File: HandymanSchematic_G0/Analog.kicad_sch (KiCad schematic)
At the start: 62 parts, among them Q1 BC847, Q2 BC847, U1 TL074, U2 TL074, U3 TL072

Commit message: rough layout
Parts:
- TP1: value AC -> AK
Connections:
- net AmpAnode: now also U2.14; no longer U2.7
- net at R19.2, R21.1: now also U2.9 (-); no longer U2.13 (-)
- net at R18.2, R20.1: now also U2.13 (-); no longer U2.6 (-)
- net at R11.1, R9.2: now also U2.6 (-); no longer U2.9 (-)
- net at R11.2, R14.1: now also U2.7; no longer U2.8
- net at C11.1, R21.2: now also U2.8; no longer U2.14
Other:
- moved on the sheet: U2B, U2C, U2D
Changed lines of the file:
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@@
 	)
 	(junction
-		(at 130.81 198.12)
-		(diameter 0)
-		(color 0 0 0 0)
-	)
-	(junction
 		(at 142.24 67.31)
 		(diameter 0)
@@
 	)
 	(junction
+		(at 181.61 200.66)
+		(diameter 0)
+		(color 0 0 0 0)
+	)
+	(junction
 		(at 49.53 67.31)
 		(diameter 0)
@@
 	)
 	(junction
+		(at 130.81 198.12)
+		(diameter 0)
+		(color 0 0 0 0)
+	)
+	(junction
+		(at 181.61 168.91)
+		(diameter 0)
+		(color 0 0 0 0)
+	)
+	(junction
 		(at 111.76 195.58)
 		(diameter 0)
@@
 	)
 	(junction
-		(at 181.61 168.91)
-		(diameter 0)
-		(color 0 0 0 0)
-	)
-	(junction
-		(at 181.61 200.66)
-		(diameter 0)
-		(color 0 0 0 0)
-	)
-	(junction
 		(at 121.92 163.83)
 		(diameter 0)
@@
 	(rectangle
 		(start 236.474 119.126)
-		(end 265.938 158.75)
+		(end 269.748 158.75)
 		(stroke
 			(width 0)
@@
 		(fields_autoplaced yes)
 		(property "Reference" "TP1"
-			(at 242.824 122.1739 0)
+			(at 243.84 122.1739 0)
 			(effects
 				(font
@@
 			)
 		)
-		(property "Value" "AC"
-			(at 242.824 124.7139 0)
+		(property "Value" "AK"
+			(at 243.84 124.7139 0)
 			(effects
 				(font
@@
 	(symbol
 		(lib_id "Amplifier_Operational:TL074")
-		(at 173.99 168.91 0)
+		(at 123.19 198.12 0)
 		(mirror x)
 		(unit 2)
@@
 		(dnp no)
 		(property "Reference" "U2"
-			(at 173.99 179.07 0)
+			(at 123.19 208.28 0)
 			(effects
 				(font
@@
 		)
 		(property "Value" "TL074"
-			(at 173.99 176.53 0)
+			(at 123.19 205.74 0)
 			(effects
 				(font
@@
 		)
 		(property "Footprint" "Package_SO:SOIC-14_3.9x8.7mm_P1.27mm"
-			(at 172.72 171.45 0)
+			(at 121.92 200.66 0)
 			(effects
 				(font
@@
 		)
 		(property "Datasheet" "http://www.ti.com/lit/ds/symlink/tl071.pdf"
-			(at 175.26 173.99 0)
+			(at 124.46 203.2 0)
 			(effects
 				(font
@@
 		)
 		(property "Description" "Quad Low-Noise JFET-Input Operational Amplifiers, DIP-14/SOIC-14"
-			(at 173.99 168.91 0)
+			(at 123.19 198.12 0)
 			(effects
 				(font
@@
 	(symbol
 		(lib_id "Amplifier_Operational:TL074")
-		(at 173.99 200.66 0)
+		(at 173.99 168.91 0)
 		(mirror x)
 		(unit 4)
@@
 		(dnp no)
 		(property "Reference" "U2"
-			(at 173.99 210.82 0)
+			(at 173.99 179.07 0)
 			(effects
 				(font
@@
 		)
 		(property "Value" "TL074"
-			(at 173.99 208.28 0)
+			(at 173.99 176.53 0)
 			(effects
 				(font
@@
 		)
 		(property "Footprint" "Package_SO:SOIC-14_3.9x8.7mm_P1.27mm"
-			(at 172.72 203.2 0)
+			(at 172.72 171.45 0)
 			(effects
 				(font
@@
 		)
 		(property "Datasheet" "http://www.ti.com/lit/ds/symlink/tl071.pdf"
-			(at 175.26 205.74 0)
+			(at 175.26 173.99 0)
 			(effects
 				(font
@@
 		)
 		(property "Description" "Quad Low-Noise JFET-Input Operational Amplifiers, DIP-14/SOIC-14"
-			(at 173.99 200.66 0)
+			(at 173.99 168.91 0)
 			(effects
 				(font
@@
 	(symbol
 		(lib_id "Amplifier_Operational:TL074")
-		(at 123.19 198.12 0)
+		(at 173.99 200.66 0)
 		(mirror x)
 		(unit 3)
@@
 		(dnp no)
 		(property "Reference" "U2"
-			(at 123.19 208.28 0)
+			(at 173.99 210.82 0)
 			(effects
 				(font
@@
 		)
 		(property "Value" "TL074"
-			(at 123.19 205.74 0)
+			(at 173.99 208.28 0)
 			(effects
 				(font
@@
 		)
 		(property "Footprint" "Package_SO:SOIC-14_3.9x8.7mm_P1.27mm"
-			(at 121.92 200.66 0)
+			(at 172.72 203.2 0)
 			(effects
 				(font
@@
 		)
 		(property "Datasheet" "http://www.ti.com/lit/ds/symlink/tl071.pdf"
-			(at 124.46 203.2 0)
+			(at 175.26 205.74 0)
 			(effects
 				(font
@@
 		)
 		(property "Description" "Quad Low-Noise JFET-Input Operational Amplifiers, DIP-14/SOIC-14"
-			(at 123.19 198.12 0)
+			(at 173.99 200.66 0)
 			(effects
 				(font

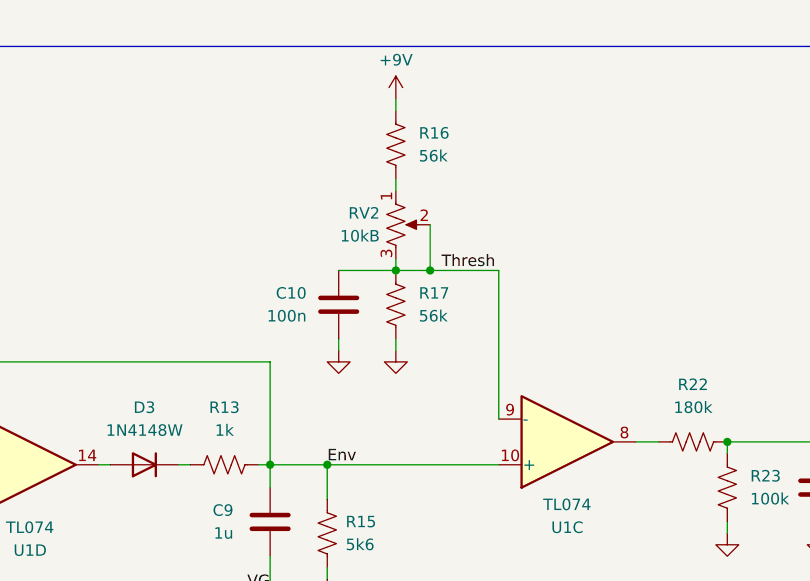
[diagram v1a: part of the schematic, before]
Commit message: removed unused components
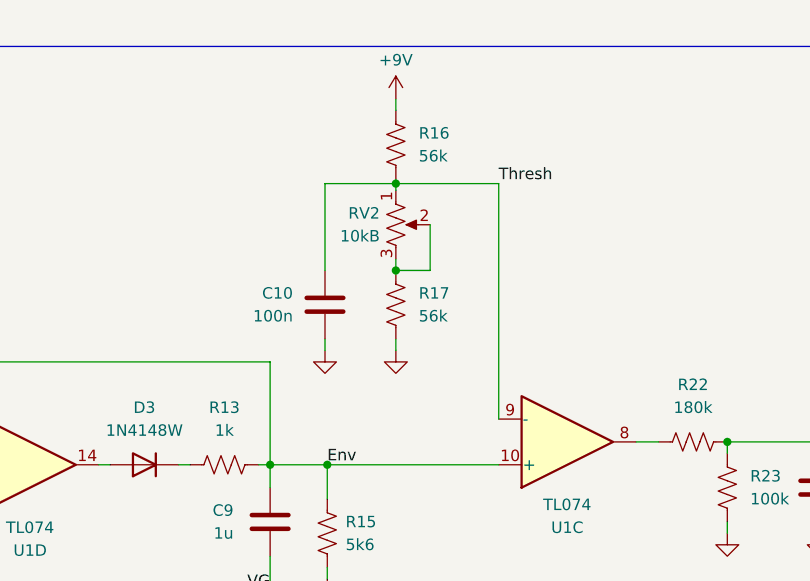
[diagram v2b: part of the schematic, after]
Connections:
- net Thresh: now also R16.2, RV2.1; no longer R17.1, RV2.2, RV2.3
- new net: R17.1, RV2.2, RV2.3
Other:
- moved on the sheet: C10
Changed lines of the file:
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@@
 	)
 	(junction
-		(at 294.132 62.23)
+		(at 149.86 36.068)
 		(diameter 0)
 		(color 0 0 0 0)
 	)
 	(junction
-		(at 69.85 201.93)
+		(at 294.132 62.23)
 		(diameter 0)
 		(color 0 0 0 0)
 	)
 	(junction
-		(at 153.67 45.72)
+		(at 69.85 201.93)
 		(diameter 0)
 		(color 0 0 0 0)
@@
 	(wire
 		(pts
-			(xy 161.29 62.23) (xy 161.29 45.72)
+			(xy 161.29 36.068) (xy 161.29 62.23)
 		)
 		(stroke
@@
 	(wire
 		(pts
-			(xy 149.86 35.56) (xy 149.86 36.83)
+			(xy 149.86 35.56) (xy 149.86 36.068)
 		)
 		(stroke
@@
 	(wire
 		(pts
-			(xy 161.29 45.72) (xy 153.67 45.72)
-		)
-		(stroke
-			(width 0)
-			(type default)
-		)
-	)
-	(wire
-		(pts
 			(xy 186.69 64.77) (xy 186.69 66.04)
 		)
@@
 	(wire
 		(pts
-			(xy 304.546 62.23) (xy 317.246 62.23)
+			(xy 161.29 36.068) (xy 149.86 36.068)
 		)
 		(stroke
@@
 	(wire
 		(pts
-			(xy 170.18 190.5) (xy 162.56 190.5)
+			(xy 304.546 62.23) (xy 317.246 62.23)
 		)
 		(stroke
@@
 	(wire
 		(pts
-			(xy 170.18 158.75) (xy 162.56 158.75)
+			(xy 170.18 190.5) (xy 162.56 190.5)
 		)
 		(stroke
@@
 	(wire
 		(pts
-			(xy 304.546 62.23) (xy 304.546 64.77)
+			(xy 170.18 158.75) (xy 162.56 158.75)
 		)
 		(stroke
@@
 	(wire
 		(pts
-			(xy 143.51 45.72) (xy 149.86 45.72)
+			(xy 304.546 62.23) (xy 304.546 64.77)
 		)
 		(stroke
@@
 	(wire
 		(pts
+			(xy 149.86 36.068) (xy 149.86 36.83)
+		)
+		(stroke
+			(width 0)
+			(type default)
+		)
+	)
+	(wire
+		(pts
 			(xy 177.8 158.75) (xy 181.61 158.75)
 		)
@@
 	(wire
 		(pts
-			(xy 143.51 53.34) (xy 143.51 54.61)
+			(xy 141.986 53.34) (xy 141.986 54.61)
 		)
 		(stroke
@@
 	(wire
 		(pts
+			(xy 141.986 45.72) (xy 141.986 36.068)
+		)
+		(stroke
+			(width 0)
+			(type default)
+		)
+	)
+	(wire
+		(pts
 			(xy 49.53 59.69) (xy 54.61 59.69)
 		)
@@
 	(wire
 		(pts
+			(xy 141.986 36.068) (xy 149.86 36.068)
+		)
+		(stroke
+			(width 0)
+			(type default)
+		)
+	)
+	(wire
+		(pts
 			(xy 107.95 93.98) (xy 125.73 93.98)
 		)
@@
 	(label "VG"
 		(at 123.19 168.91 180)
+		(fields_autoplaced yes)
 		(effects
 			(font
@@
 	(label "VG"
 		(at 135.89 81.28 180)
+		(fields_autoplaced yes)
 		(effects
 			(font
@@
 	(label "AmpAnode"
 		(at 246.126 133.604 0)
+		(fields_autoplaced yes)
 		(effects
 			(font
@@
 	(label "VG"
 		(at 95.25 177.8 0)
+		(fields_autoplaced yes)
 		(effects
 			(font
@@
 	(label "VG"
 		(at 50.8 72.39 180)
+		(fields_autoplaced yes)
 		(effects
 			(font
@@
 	(label "Env"
 		(at 142.24 67.31 0)
+		(fields_autoplaced yes)
 		(effects
 			(font
@@
 		)
 	)
-	(label "HalfRect"
-		(at 80.01 60.96 0)
+	(label "Thresh"
+		(at 161.29 36.068 0)
+		(fields_autoplaced yes)
 		(effects
 			(font
@@
 		)
 	)
-	(label "VG"
-		(at 142.24 90.17 180)
+	(label "HalfRect"
+		(at 80.01 60.96 0)
+		(fields_autoplaced yes)
 		(effects
 			(font
 				(size 1.27 1.27)
 			)
-			(justify right bottom)
+			(justify left bottom)
 		)
 	)
 	(label "VG"
-		(at 95.25 82.55 180)
+		(at 142.24 90.17 180)
+		(fields_autoplaced yes)
 		(effects
 			(font
@@
 		)
 	)
-	(label "Thresh"
-		(at 154.94 45.72 0)
+	(label "VG"
+		(at 95.25 82.55 180)
+		(fields_autoplaced yes)
 		(effects
 			(font
 				(size 1.27 1.27)
 			)
-			(justify left bottom)
+			(justify right bottom)
 		)
 	)
 	(label "AmpAnode"
 		(at 153.67 217.17 180)
+		(fields_autoplaced yes)
 		(effects
 			(font
@@
 	(label "AmpCathode"
 		(at 142.24 166.37 0)
+		(fields_autoplaced yes)
 		(effects
 			(font
@@
 	(label "VG"
 		(at 276.352 64.77 180)
+		(fields_autoplaced yes)
 		(effects
 			(font
@@
 	(label "SumPt"
 		(at 140.97 198.12 0)
+		(fields_autoplaced yes)
 		(effects
 			(font
@@
 	(label "VG"
 		(at 166.37 203.2 180)
+		(fields_autoplaced yes)
 		(effects
 			(font
@@
 	(label "VG"
 		(at 166.37 171.45 180)
+		(fields_autoplaced yes)
 		(effects
 			(font
@@
 	(label "VG"
 		(at 246.126 148.082 0)
+		(fields_autoplaced yes)
 		(effects
 			(font
@@
 	(label "VG"
 		(at 317.246 67.31 180)
+		(fields_autoplaced yes)
 		(effects
 			(font
@@
 	(label "Env"
 		(at 246.126 154.686 0)
+		(fields_autoplaced yes)
 		(effects
 			(font
@@
 	(label "VG"
 		(at 125.73 101.6 0)
+		(fields_autoplaced yes)
 		(effects
 			(font
@@
 	(label "VG"
 		(at 115.57 200.66 180)
+		(fields_autoplaced yes)
 		(effects
 			(font
@@
 	(label "Thresh"
 		(at 246.126 141.224 0)
+		(fields_autoplaced yes)
 		(effects
 			(font
@@
 	(label "VG"
 		(at 304.546 72.644 180)
+		(fields_autoplaced yes)
 		(effects
 			(font
@@
 	(label "AmpCathode"
 		(at 246.126 126.746 0)
+		(fields_autoplaced yes)
 		(effects
 			(font
@@
 	(symbol
 		(lib_id "power:GND")
-		(at 143.51 54.61 0)
+		(at 141.986 54.61 0)
 		(unit 1)
 		(exclude_from_sim no)
@@
 		(fields_autoplaced yes)
 		(property "Reference" "#PWR015"
-			(at 143.51 60.96 0)
+			(at 141.986 60.96 0)
 			(effects
 				(font
@@
 		)
 		(property "Value" "GND"
-			(at 143.51 58.42 0)
+			(at 141.986 58.42 0)
 			(effects
 				(font
@@
 		)
 		(property "Footprint" ""
-			(at 143.51 54.61 0)
+			(at 141.986 54.61 0)
 			(effects
 				(font
@@
 		)
 		(property "Datasheet" ""
-			(at 143.51 54.61 0)
+			(at 141.986 54.61 0)
 			(effects
 				(font
@@
 		)
 		(property "Description" "Power symbol creates a global label with name \"GND\" , ground"
-			(at 143.51 54.61 0)
+			(at 141.986 54.61 0)
 			(effects
 				(font
@@
 	(symbol
 		(lib_id "Device:C")
-		(at 143.51 49.53 0)
+		(at 141.986 49.53 0)
 		(unit 1)
 		(exclude_from_sim no)
@@
 		(fields_autoplaced yes)
 		(property "Reference" "C10"
-			(at 139.954 48.2599 0)
+			(at 138.43 48.2599 0)
 			(effects
 				(font
@@
 		)
 		(property "Value" "100n"
-			(at 139.954 50.7999 0)
+			(at 138.43 50.7999 0)
 			(effects
 				(font
@@
 		)
 		(property "Footprint" "Capacitor_SMD:C_0805_2012Metric"
-			(at 144.4752 53.34 0)
+			(at 142.9512 53.34 0)
 			(effects
 				(font
@@
 		)
 		(property "Datasheet" "~"
-			(at 143.51 49.53 0)
+			(at 141.986 49.53 0)
 			(effects
 				(font
@@
 		)
 		(property "Description" "Unpolarized capacitor"
-			(at 143.51 49.53 0)
+			(at 141.986 49.53 0)
 			(effects
 				(font

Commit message: board outline for 1590B size
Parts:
- removed TP1: AK, TestPoint:TestPoint_THTPad_D2.0mm_Drill1.0mm_VAL, symbol Connector:TestPoint
- removed TP2: AA, TestPoint:TestPoint_THTPad_D2.0mm_Drill1.0mm_VAL, symbol Connector:TestPoint
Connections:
- no-connect marks 1 -> 0
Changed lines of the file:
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@@
 		(color 0 0 0 0)
 	)
-	(no_connect
-		(at 124.46 107.95)
-	)
 	(wire
 		(pts
@@
 	(wire
 		(pts
-			(xy 241.3 133.604) (xy 246.126 133.604)
-		)
-		(stroke
-			(width 0)
-			(type default)
-		)
-	)
-	(wire
-		(pts
 			(xy 342.646 64.77) (xy 348.234 64.77)
 		)
@@
 		(pts
 			(xy 50.8 67.31) (xy 49.53 67.31)
-		)
-		(stroke
-			(width 0)
-			(type default)
-		)
-	)
-	(wire
-		(pts
-			(xy 241.3 126.746) (xy 246.126 126.746)
 		)
 		(stroke
@@
 	)
 	(rectangle
-		(start 236.474 119.126)
+		(start 236.474 133.985)
 		(end 269.748 158.75)
 		(stroke
@@
 	(text "Test Points"
 		(exclude_from_sim no)
-		(at 236.474 116.332 0)
+		(at 235.458 130.81 0)
 		(effects
 			(font
@@
 	(label "VG"
 		(at 123.19 168.91 180)
-		(fields_autoplaced yes)
 		(effects
 			(font
@@
 	(label "VG"
 		(at 135.89 81.28 180)
-		(fields_autoplaced yes)
 		(effects
 			(font
@@
 			)
 			(justify right bottom)
-		)
-	)
-	(label "AmpAnode"
-		(at 246.126 133.604 0)
-		(fields_autoplaced yes)
-		(effects
-			(font
-				(size 1.27 1.27)
-			)
-			(justify left bottom)
 		)
 	)
 	(label "VG"
 		(at 95.25 177.8 0)
-		(fields_autoplaced yes)
 		(effects
 			(font
@@
 	(label "VG"
 		(at 50.8 72.39 180)
-		(fields_autoplaced yes)
 		(effects
 			(font
@@
 	(label "Env"
 		(at 142.24 67.31 0)
-		(fields_autoplaced yes)
 		(effects
 			(font
@@
 	(label "Thresh"
 		(at 161.29 36.068 0)
-		(fields_autoplaced yes)
 		(effects
 			(font
@@
 	(label "HalfRect"
 		(at 80.01 60.96 0)
-		(fields_autoplaced yes)
 		(effects
 			(font
@@
 	(label "VG"
 		(at 142.24 90.17 180)
-		(fields_autoplaced yes)
 		(effects
 			(font
@@
 	(label "VG"
 		(at 95.25 82.55 180)
-		(fields_autoplaced yes)
 		(effects
 			(font
@@
 	(label "AmpAnode"
 		(at 153.67 217.17 180)
-		(fields_autoplaced yes)
 		(effects
 			(font
@@
 	(label "AmpCathode"
 		(at 142.24 166.37 0)
-		(fields_autoplaced yes)
 		(effects
 			(font
@@
 	(label "VG"
 		(at 276.352 64.77 180)
-		(fields_autoplaced yes)
 		(effects
 			(font
@@
 	(label "SumPt"
 		(at 140.97 198.12 0)
-		(fields_autoplaced yes)
 		(effects
 			(font
@@
 	(label "VG"
 		(at 166.37 203.2 180)
-		(fields_autoplaced yes)
 		(effects
 			(font
@@
 	(label "VG"
 		(at 166.37 171.45 180)
-		(fields_autoplaced yes)
 		(effects
 			(font
@@
 	(label "VG"
 		(at 246.126 148.082 0)
-		(fields_autoplaced yes)
 		(effects
 			(font
@@
 	(label "VG"
 		(at 317.246 67.31 180)
-		(fields_autoplaced yes)
 		(effects
 			(font
@@
 	(label "Env"
 		(at 246.126 154.686 0)
-		(fields_autoplaced yes)
 		(effects
 			(font
@@
 	(label "VG"
 		(at 125.73 101.6 0)
-		(fields_autoplaced yes)
 		(effects
 			(font
@@
 	(label "VG"
 		(at 115.57 200.66 180)
-		(fields_autoplaced yes)
 		(effects
 			(font
@@
 	(label "Thresh"
 		(at 246.126 141.224 0)
-		(fields_autoplaced yes)
 		(effects
 			(font
@@
 	(label "VG"
 		(at 304.546 72.644 180)
-		(fields_autoplaced yes)
 		(effects
 			(font
@@
 			)
 			(justify right bottom)
-		)
-	)
-	(label "AmpCathode"
-		(at 246.126 126.746 0)
-		(fields_autoplaced yes)
-		(effects
-			(font
-				(size 1.27 1.27)
-			)
-			(justify left bottom)
 		)
 	)
@@
 	)
 	(symbol
-		(lib_id "Connector:TestPoint")
-		(at 241.3 133.604 0)
-		(unit 1)
-		(exclude_from_sim no)
-		(in_bom no)
-		(on_board yes)
-		(dnp no)
-		(fields_autoplaced yes)
-		(property "Reference" "TP2"
-			(at 242.824 129.0319 0)
-			(effects
-				(font
-					(size 1.27 1.27)
-				)
-				(justify left)
-			)
-		)
-		(property "Value" "AA"
-			(at 242.824 131.5719 0)
-			(effects
-				(font
-					(size 1.27 1.27)
-				)
-				(justify left)
-			)
-		)
-		(property "Footprint" "TestPoint:TestPoint_THTPad_D2.0mm_Drill1.0mm_VAL"
-			(at 246.38 133.604 0)
-			(effects
-				(font
-					(size 1.27 1.27)
-				)
-				(hide yes)
-			)
-		)
-		(property "Datasheet" "~"
-			(at 246.38 133.604 0)
-			(effects
-				(font
-					(size 1.27 1.27)
-				)
-				(hide yes)
-			)
-		)
-		(property "Description" "test point"
-			(at 241.3 133.604 0)
-			(effects
-				(font
-					(size 1.27 1.27)
-				)
-				(hide yes)
-			)
-		)
-		(pin "1"
-		)
-		(instances
-			(project "HandymanSchematic_G0"
-				(path "/bc3da82e-d0a7-49a6-b9ec-ecd2040670ff/3aa5a90d-1712-4ed6-8a31-c8d55dd0f37d"
-					(reference "TP2")
-					(unit 1)
-				)
-			)
-		)
-	)
-	(symbol
 		(lib_id "Diode:1N4148W")
 		(at 58.42 59.69 0)
@@
 					(unit 1)
 				)
-			)
-		)
-	)
-	(symbol
-		(lib_id "Connector:TestPoint")
-		(at 241.3 126.746 0)
-		(unit 1)
-		(exclude_from_sim no)
-		(in_bom no)
-		(on_board yes)
-		(dnp no)
-		(fields_autoplaced yes)
-		(property "Reference" "TP1"
-			(at 243.84 122.1739 0)
-			(effects
-				(font
-					(size 1.27 1.27)
-				)
-				(justify left)
-			)
-		)
-		(property "Value" "AK"
-			(at 243.84 124.7139 0)
-			(effects
-				(font
-					(size 1.27 1.27)
-				)
-				(justify left)
-			)
-		)
-		(property "Footprint" "TestPoint:TestPoint_THTPad_D2.0mm_Drill1.0mm_VAL"
-			(at 246.38 126.746 0)
-			(effects
-				(font
-					(size 1.27 1.27)
-				)
-				(hide yes)
-			)
-		)
-		(property "Datasheet" "~"
-			(at 246.38 126.746 0)
-			(effects
-				(font
-					(size 1.27 1.27)
-				)
-				(hide yes)
-			)
-		)
-		(property "Description" "test point"
-			(at 241.3 126.746 0)
-			(effects
-				(font
-					(size 1.27 1.27)
-				)
-				(hide yes)
-			)
-		)
-		(pin "1"
-		)
-		(instances
-			(project "HandymanSchematic_G0"
-				(path "/bc3da82e-d0a7-49a6-b9ec-ecd2040670ff/3aa5a90d-1712-4ed6-8a31-c8d55dd0f37d"
-					(reference "TP1")
-					(unit 1)
-				)
